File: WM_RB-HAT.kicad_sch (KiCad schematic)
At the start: 85 parts, among them J1 AudioJack3, J2 AudioJack3, J3 2x20 Pins, J4 AudioJack3, J5 AudioJack3, J6 Audio In, J7 Audio Out, Q1 BC817, Q2 BFS17A, SW1 SSSS213202, U1 WM8960, U3 74AHC1G14, U4 MCP1711T-33 /OT, X1 XO32, Y1 24MHz

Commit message: Zone clearance 0.3→0.2mm, add silkscreen SVGs
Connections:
- net INPUT_L: no longer J5.R
- net INPUT_R: no longer J1.R
- net OUT_MONO_AC: no longer J2.R
- no-connect marks 29 -> 32
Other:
- moved on the sheet: C18, C19, C20, C21, FB1, FB2, R10, R15, R7, R8, R9, SW1

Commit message: Add revision R0.2, update title
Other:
- title: Raspberry Audio Hat  -> Weird Audio HAT
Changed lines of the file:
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@@
 	(paper "A3")
 	(title_block
-		(title "Raspberry Audio Hat ")
+		(title "Weird Audio HAT")
 		(date "2024-04-19")
-		(rev "A")
+		(rev "R0.2")
 	)
 	(text "INPUTS"

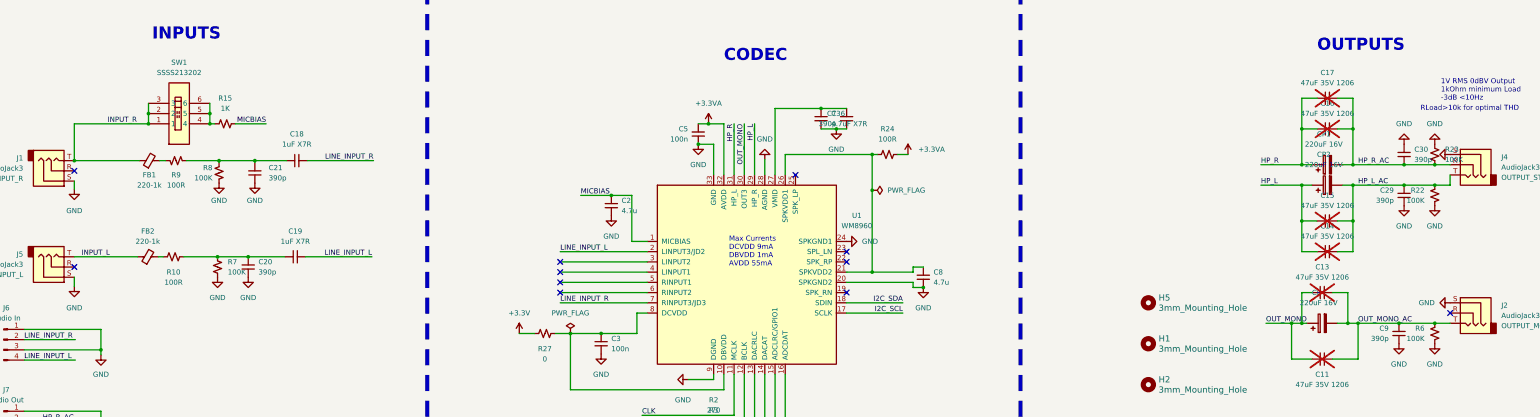
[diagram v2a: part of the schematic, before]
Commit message: R1.1: HP output filter 100k→0Ω, silk labels OUT L/R, MIC-R BIAS
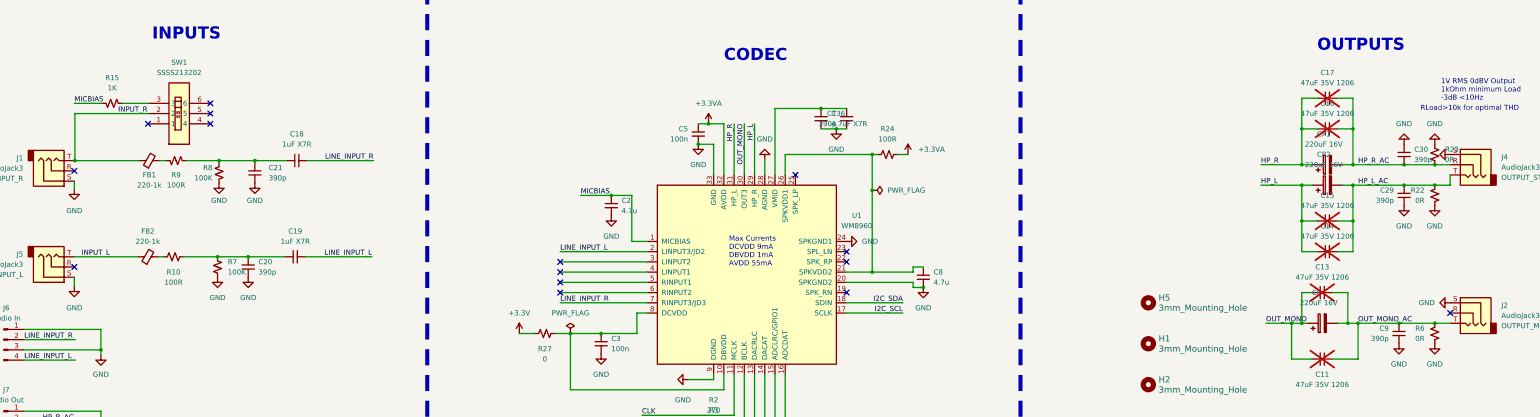
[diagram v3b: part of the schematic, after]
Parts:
- R22, R23, R6: value 100K -> 0R; LCSC C25803 -> C21189
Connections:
- net INPUT_R: no longer SW1.1, SW1.3
- new net: R15.1, SW1.3
- now unconnected: SW1.4, SW1.5, SW1.6
- no-connect marks 32 -> 36
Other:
- moved on the sheet: R15
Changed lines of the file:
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@@
 	)
 	(junction
-		(at 59.055 125.73)
-		(diameter 0)
-		(color 0 0 0 0)
-	)
-	(junction
 		(at 378.46 177.8)
 		(diameter 0)
@@
 	)
 	(junction
-		(at 74.295 125.73)
-		(diameter 0)
-		(color 0 0 0 0)
-	)
-	(junction
 		(at 238.76 144.78)
 		(diameter 0)
@@
 	)
 	(junction
-		(at 74.295 128.27)
-		(diameter 0)
-		(color 0 0 0 0)
-	)
-	(junction
 		(at 173.99 146.05)
 		(diameter 0)
@@
 	)
 	(junction
-		(at 40.64 137.414)
-		(diameter 0)
-		(color 0 0 0 0)
-	)
-	(junction
 		(at 76.2 161.29)
 		(diameter 0)
@@
 	)
 	(junction
+		(at 40.767 137.414)
+		(diameter 0)
+		(color 0 0 0 0)
+	)
+	(junction
 		(at 345.44 138.43)
 		(diameter 0)
@@
 	)
 	(junction
-		(at 59.055 128.27)
-		(diameter 0)
-		(color 0 0 0 0)
-	)
-	(junction
 		(at 358.14 152.4)
 		(diameter 0)
@@
 	)
 	(no_connect
+		(at 74.422 128.27)
+	)
+	(no_connect
 		(at 228.6 53.34)
 	)
@@
 	)
 	(no_connect
+		(at 74.422 123.19)
+	)
+	(no_connect
 		(at 161.29 170.18)
 	)
 	(no_connect
+		(at 74.422 125.73)
+	)
+	(no_connect
 		(at 185.42 53.34)
 	)
@@
 	)
 	(no_connect
+		(at 58.928 128.27)
+	)
+	(no_connect
 		(at 232.41 170.18)
 	)
@@
 	(wire
 		(pts
-			(xy 74.295 128.27) (xy 75.565 128.27)
-		)
-		(stroke
-			(width 0)
-			(type default)
-		)
-	)
-	(wire
-		(pts
 			(xy 26.67 44.45) (xy 34.29 44.45)
 		)
@@
 	(wire
 		(pts
-			(xy 207.01 190.5) (xy 207.01 203.2)
+			(xy 52.578 123.19) (xy 59.055 123.19)
 		)
 		(stroke
@@
 	(wire
 		(pts
-			(xy 74.295 123.19) (xy 74.295 125.73)
+			(xy 207.01 190.5) (xy 207.01 203.2)
 		)
 		(stroke
@@
 	(wire
 		(pts
-			(xy 40.64 128.27) (xy 40.64 137.414)
-		)
-		(stroke
-			(width 0)
-			(type default)
-		)
-	)
-	(wire
-		(pts
 			(xy 47.244 184.404) (xy 28.194 184.404)
 		)
@@
 	(wire
 		(pts
-			(xy 71.12 52.07) (xy 73.66 52.07)
+			(xy 40.767 137.414) (xy 56.769 137.414)
 		)
 		(stroke
@@
 	(wire
 		(pts
-			(xy 358.14 160.02) (xy 358.14 152.4)
+			(xy 71.12 52.07) (xy 73.66 52.07)
 		)
 		(stroke
@@
 	(wire
 		(pts
-			(xy 181.61 210.82) (xy 209.55 210.82)
+			(xy 358.14 160.02) (xy 358.14 152.4)
 		)
 		(stroke
@@
 	(wire
 		(pts
-			(xy 74.295 125.73) (xy 74.295 128.27)
+			(xy 181.61 210.82) (xy 209.55 210.82)
 		)
 		(stroke
@@
 	(wire
 		(pts
-			(xy 40.64 128.27) (xy 59.055 128.27)
-		)
-		(stroke
-			(width 0)
-			(type default)
-		)
-	)
-	(wire
-		(pts
 			(xy 378.46 143.51) (xy 370.84 143.51)
 		)
@@
 	(wire
 		(pts
-			(xy 59.055 123.19) (xy 59.055 125.73)
-		)
-		(stroke
-			(width 0)
-			(type default)
-		)
-	)
-	(wire
-		(pts
 			(xy 185.42 38.1) (xy 170.18 38.1)
 		)
@@
 	(wire
 		(pts
+			(xy 47.498 123.19) (xy 40.64 123.19)
+		)
+		(stroke
+			(width 0)
+			(type default)
+		)
+	)
+	(wire
+		(pts
 			(xy 217.17 140.97) (xy 217.17 135.89)
 		)
@@
 	(wire
 		(pts
-			(xy 40.64 137.414) (xy 56.769 137.414)
-		)
-		(stroke
-			(width 0)
-			(type default)
-		)
-	)
-	(wire
-		(pts
 			(xy 201.93 208.28) (xy 209.55 208.28)
 		)
@@
 	(wire
 		(pts
-			(xy 59.055 125.73) (xy 59.055 128.27)
-		)
-		(stroke
-			(width 0)
-			(type default)
-		)
-	)
-	(wire
-		(pts
 			(xy 358.14 138.43) (xy 370.84 138.43)
 		)
@@
 	(wire
 		(pts
+			(xy 40.767 125.73) (xy 40.767 137.414)
+		)
+		(stroke
+			(width 0)
+			(type default)
+		)
+	)
+	(wire
+		(pts
 			(xy 26.67 50.8) (xy 26.67 52.07)
 		)
@@
 	(wire
 		(pts
+			(xy 74.295 125.73) (xy 74.422 125.73)
+		)
+		(stroke
+			(width 0)
+			(type default)
+		)
+	)
+	(wire
+		(pts
 			(xy 354.33 121.92) (xy 358.14 121.92)
 		)
@@
 	(wire
 		(pts
-			(xy 80.645 128.27) (xy 88.265 128.27)
+			(xy 40.767 125.73) (xy 59.055 125.73)
 		)
 		(stroke
@@
 	(wire
 		(pts
+			(xy 40.767 137.414) (xy 40.64 137.414)
+		)
+		(stroke
+			(width 0)
+			(type default)
+		)
+	)
+	(wire
+		(pts
 			(xy 209.55 190.5) (xy 209.55 208.28)
 		)
@@
 		)
 	)
+	(label "MICBIAS"
+		(at 40.64 123.19 0)
+		(effects
+			(font
+				(size 1.27 1.27)
+			)
+			(justify left bottom)
+		)
+	)
 	(label "I2S_CLK"
 		(at 243.84 48.26 180)
@@
 		)
 	)
-	(label "MICBIAS"
-		(at 88.265 128.27 180)
-		(effects
-			(font
-				(size 1.27 1.27)
-			)
-			(justify right bottom)
-		)
-	)
 	(label "CLK"
 		(at 181.61 200.66 0)
@@
 	)
 	(label "INPUT_R"
-		(at 48.895 128.27 0)
+		(at 58.801 125.73 180)
 		(effects
 			(font
 				(size 1.27 1.27)
 			)
-			(justify left bottom)
+			(justify right bottom)
 		)
 	)
@@
 		(on_board yes)
 		(dnp no)
+		(fields_autoplaced yes)
 		(property "Reference" "#PWR02"
 			(at 375.92 135.89 0)
@@
 			)
 		)
-		(property "Value" "100K"
+		(property "Value" "0R"
 			(at 381 137.1599 0)
 			(effects
@@
 			)
 		)
-		(property "LCSC" "C25803"
+		(property "LCSC" "C21189"
 			(at 378.46 135.89 0)
 			(effects
@@
 			)
 		)
-		(property "Value" "100K"
+		(property "Value" "0R"
 			(at 375.92 181.6099 0)
 			(effects
@@
 			)
 		)
-		(property "LCSC" "C25803"
+		(property "LCSC" "C21189"
 			(at 0 0 0)
 			(effects
@@
 	(symbol
 		(lib_id "Device:R_Small_US")
-		(at 78.105 128.27 90)
+		(at 50.038 123.19 270)
+		(mirror x)
 		(unit 1)
 		(exclude_from_sim no)
@@
 		(fields_autoplaced yes)
 		(property "Reference" "R15"
-			(at 78.105 121.92 90)
+			(at 50.038 116.84 90)
 			(effects
 				(font
@@
 		)
 		(property "Value" "1K"
-			(at 78.105 124.46 90)
+			(at 50.038 119.38 90)
 			(effects
 				(font
@@
 		)
 		(property "Footprint" "Resistor_SMD:R_0603_1608Metric"
-			(at 78.105 128.27 0)
+			(at 50.038 123.19 0)
 			(effects
 				(font
@@
 		)
 		(property "Datasheet" "~"
-			(at 78.105 128.27 0)
+			(at 50.038 123.19 0)
 			(effects
 				(font
@@
 		)
 		(property "Description" ""
-			(at 78.105 128.27 0)
+			(at 50.038 123.19 0)
 			(effects
 				(font
@@
 		)
 		(property "Elemon1" ""
-			(at 78.105 128.27 0)
+			(at 50.038 123.19 0)
 			(effects
 				(font
@@
 		)
 		(property "LCSC" "C21190"
-			(at 78.105 128.27 0)
+			(at 50.038 123.19 0)
 			(effects
 				(font
@@
 			)
 		)
-		(property "Value" "100K"
+		(property "Value" "0R"
 			(at 375.92 147.3199 0)
 			(effects
@@
 			)
 		)
-		(property "LCSC" "C25803"
+		(property "LCSC" "C21189"
 			(at 0 0 0)
 			(effects

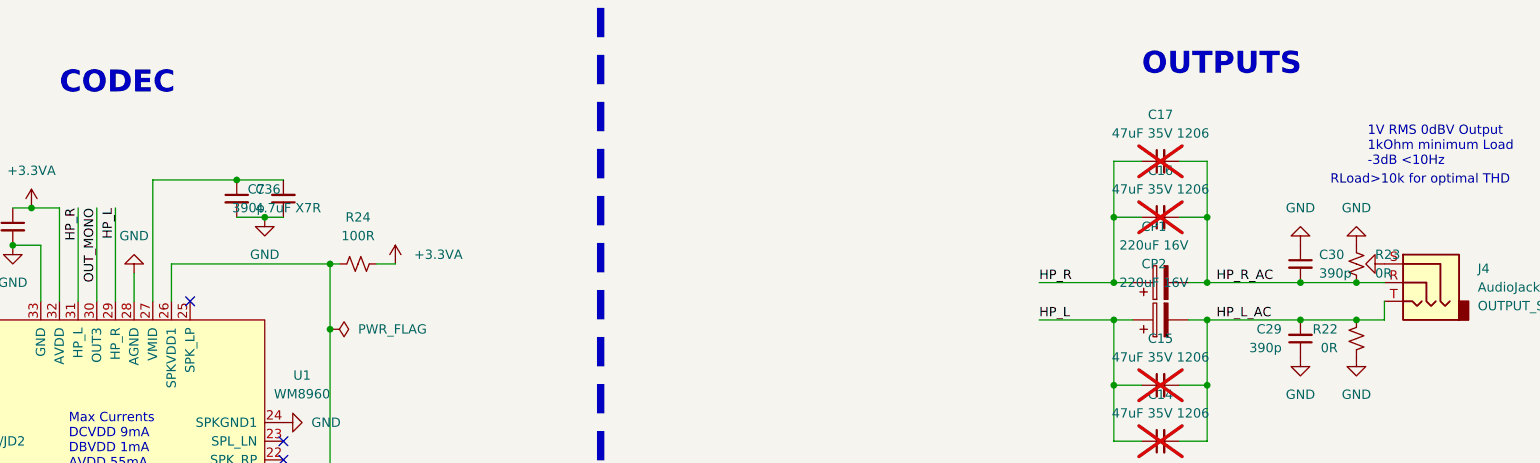
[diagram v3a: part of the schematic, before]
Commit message: Migrate project to KiCad 10 format
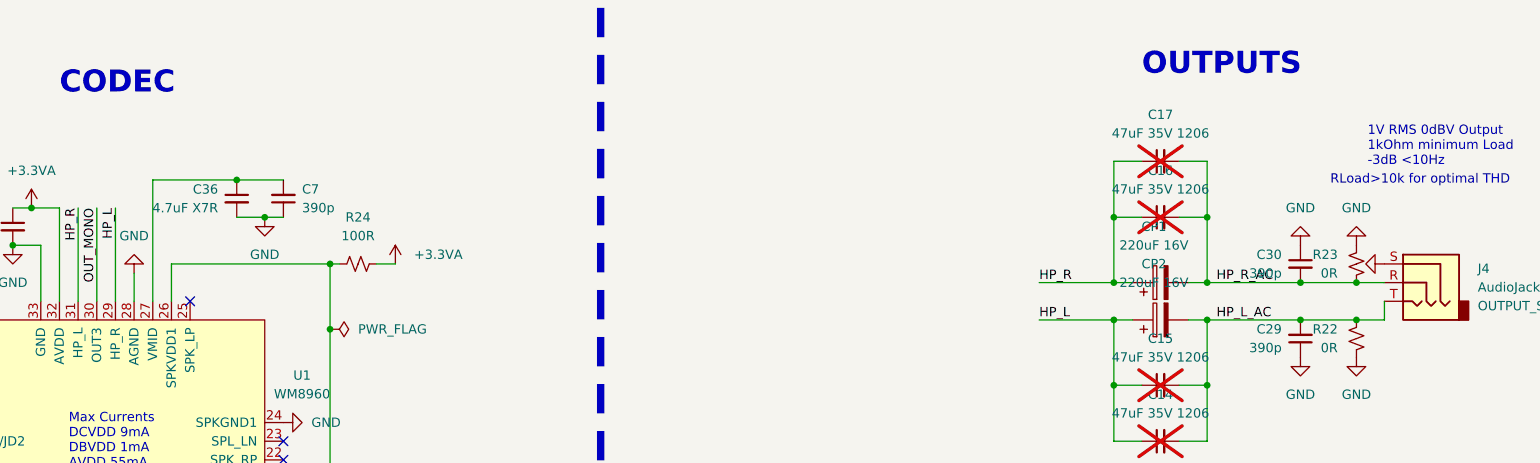
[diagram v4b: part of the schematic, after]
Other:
- moved on the sheet: C7

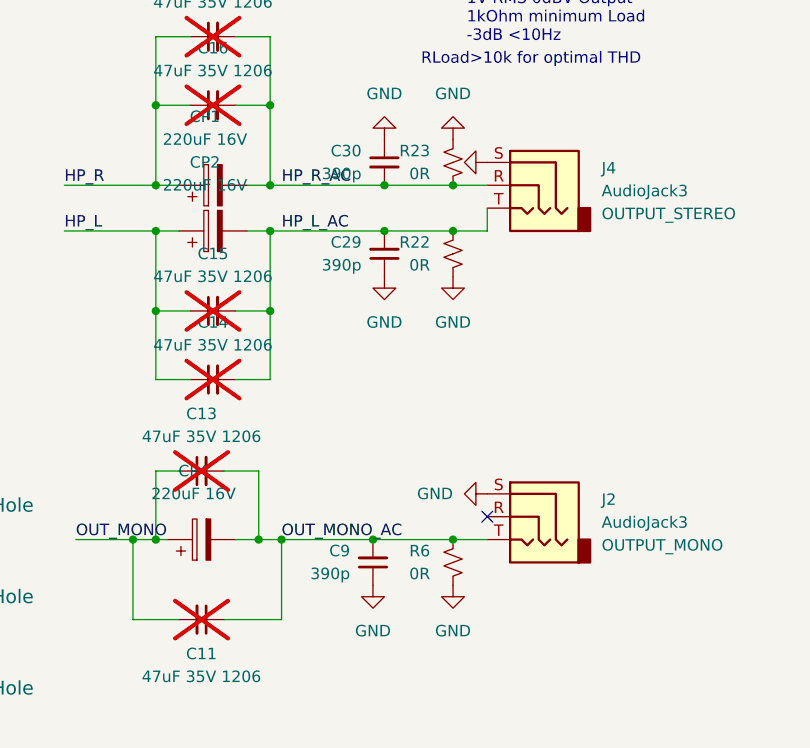
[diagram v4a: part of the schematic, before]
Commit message: Set R6/R22/R23 to 100K (fix output short, restore original bleed)
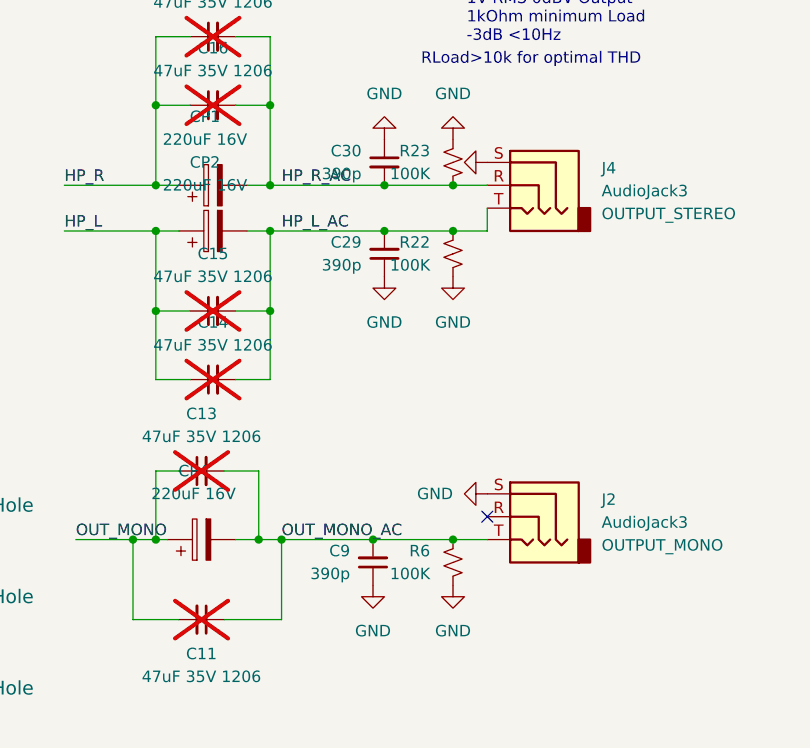
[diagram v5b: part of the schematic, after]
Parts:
- R22, R23, R6: value 0R -> 100K
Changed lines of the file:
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@@
 			)
 		)
-		(property "Value" "0R"
+		(property "Value" "100K"
 			(at 375.92 137.1599 0)
 			(show_name no)
@@
 			)
 		)
-		(property "Value" "0R"
+		(property "Value" "100K"
 			(at 375.92 181.6099 0)
 			(show_name no)
@@
 			)
 		)
-		(property "Value" "0R"
+		(property "Value" "100K"
 			(at 375.92 147.3199 0)
 			(show_name no)
